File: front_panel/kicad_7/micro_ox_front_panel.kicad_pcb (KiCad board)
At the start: 2 copper layers, 323.8 x 177.8 mm, 8 parts

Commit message: Progress on circuit boards
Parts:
- removed REF** (x8): MountingHole_3.2mm_M3_DIN965, MountingHole:MountingHole_3.2mm_M3_DIN965
- added H1: MountingHole_Pad, MountingHole:MountingHole_3.2mm_M3_Pad_Via, F.Cu at (54.6, 47.0)
- added H2: MountingHole_Pad, MountingHole:MountingHole_3.2mm_M3_Pad_Via, F.Cu at (54.6, 131.4)
- added H3: MountingHole_Pad, MountingHole:MountingHole_3.2mm_M3_Pad_Via, F.Cu at (54.6, 215.9)
- added H4: MountingHole_Pad, MountingHole:MountingHole_3.2mm_M3_Pad_Via, F.Cu at (221.0, 47.0)
- added H5: MountingHole_Pad, MountingHole:MountingHole_3.2mm_M3_Pad_Via, F.Cu at (229.9, 215.9)
- added H6: MountingHole_Pad, MountingHole:MountingHole_3.2mm_M3_Pad_Via, F.Cu at (369.6, 47.0)
- added H7: MountingHole_Pad, MountingHole:MountingHole_3.2mm_M3_Pad_Via, F.Cu at (369.6, 131.4)
- added H8: MountingHole_Pad, MountingHole:MountingHole_3.2mm_M3_Pad_Via, F.Cu at (369.6, 215.9)
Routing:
- added copper zone on B.Cu, net GND
- added copper zone on F.Cu, net GND
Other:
- outline, holes or cut-outs redrawn

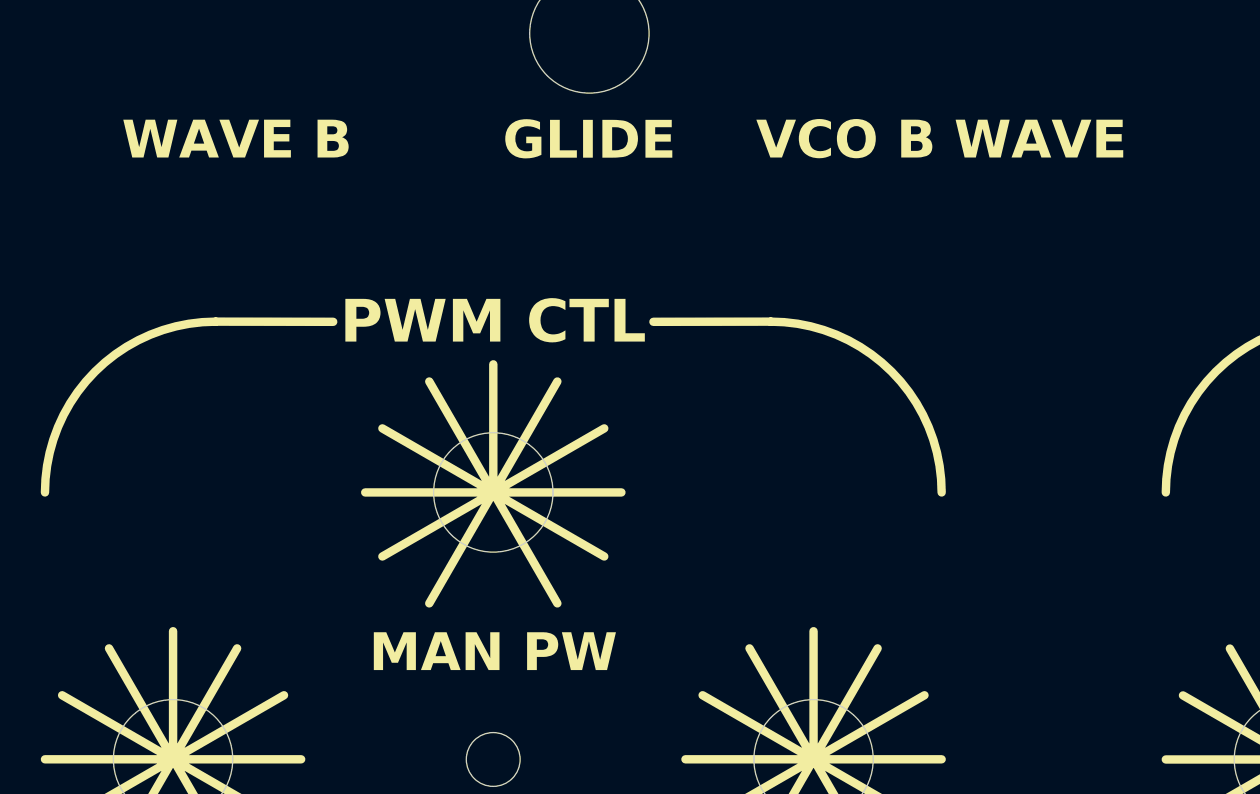
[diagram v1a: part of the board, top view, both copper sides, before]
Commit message: Tweaks to front panel, fix some copy-paste errors
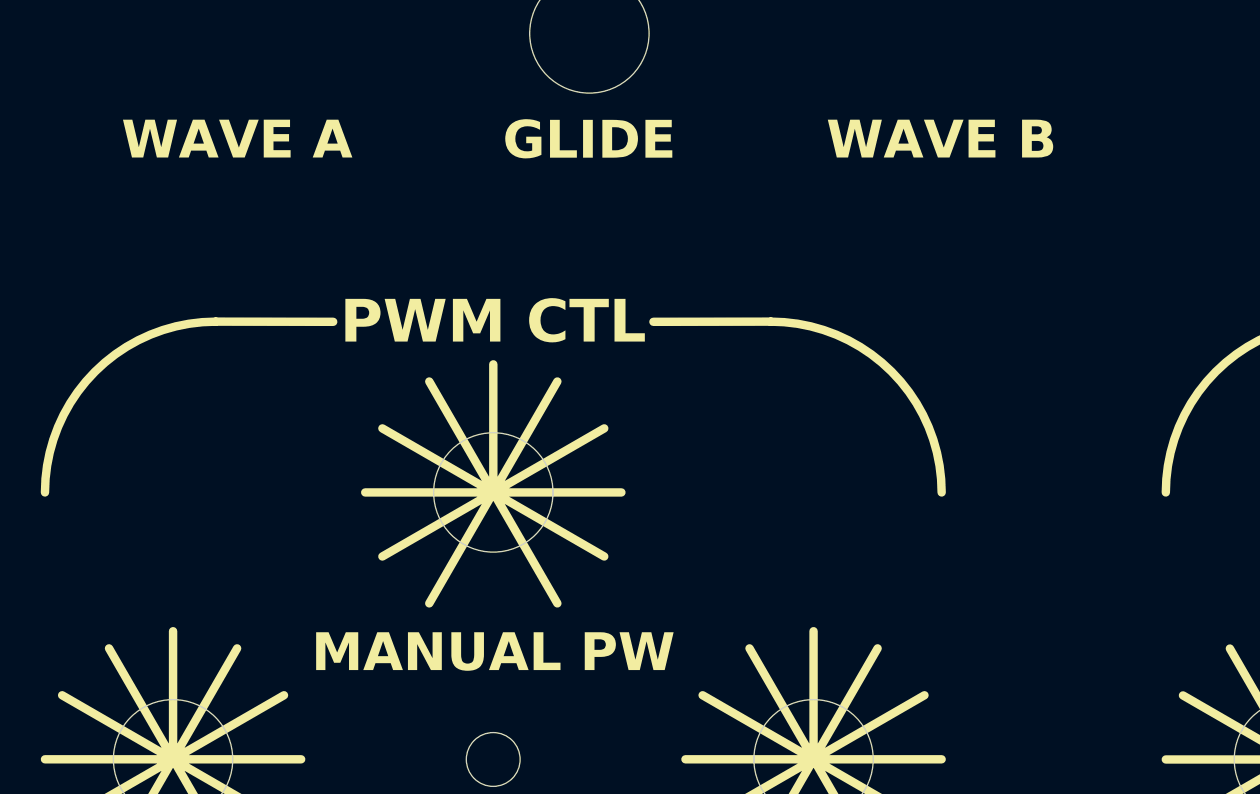
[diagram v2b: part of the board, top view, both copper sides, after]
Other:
- board text added: "MANUAL PW"
- board text added: "WAVE A"
- board text removed: "MAN PW"
- board text removed: "VCO B WAVE"

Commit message: Update front panel
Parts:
- moved H6 3.18 mm to (372.7, 47.0)
- moved H7 3.18 mm to (372.7, 131.4)
- moved H8 3.18 mm to (372.7, 215.9)
- moved H1 3.17 mm to (51.4, 47.0)
- moved H2 3.17 mm to (51.4, 131.4)
- moved H3 3.17 mm to (51.4, 215.9)
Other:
- board size 323.8 x 177.8 mm -> 330.2 x 177.8 mm
- board text added: "JLCJLCJLCJLC"
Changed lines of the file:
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@@
   (title_block
     (title "Micro-Ox front panel")
-    (date "2023-04-13")
+    (date "2023-04-23")
     (rev "0")
     (comment 1 "creativecommons.org/licenses/by/4.0/")
@@
   (net 1 "GND")
   (footprint "MountingHole:MountingHole_3.2mm_M3_Pad_Via" (layer "F.Cu")
-    (at 54.61 131.445)
+    (at 51.435 131.445)
     (descr "Mounting Hole 3.2mm, M3")
     (tags "mounting hole 3.2mm m3")
@@
   )
   (footprint "MountingHole:MountingHole_3.2mm_M3_Pad_Via" (layer "F.Cu")
-    (at 54.61 46.99)
+    (at 51.435 46.99)
     (descr "Mounting Hole 3.2mm, M3")
     (tags "mounting hole 3.2mm m3")
@@
   )
   (footprint "MountingHole:MountingHole_3.2mm_M3_Pad_Via" (layer "F.Cu")
-    (at 369.57 215.9)
+    (at 372.745 215.9)
     (descr "Mounting Hole 3.2mm, M3")
     (tags "mounting hole 3.2mm m3")
@@
   )
   (footprint "MountingHole:MountingHole_3.2mm_M3_Pad_Via" (layer "F.Cu")
-    (at 369.57 46.99)
+    (at 372.745 46.99)
     (descr "Mounting Hole 3.2mm, M3")
     (tags "mounting hole 3.2mm m3")
@@
   )
   (footprint "MountingHole:MountingHole_3.2mm_M3_Pad_Via" (layer "F.Cu")
-    (at 54.61 215.9)
+    (at 51.435 215.9)
     (descr "Mounting Hole 3.2mm, M3")
     (tags "mounting hole 3.2mm m3")
@@
   )
   (footprint "MountingHole:MountingHole_3.2mm_M3_Pad_Via" (layer "F.Cu")
-    (at 369.57 131.445)
+    (at 372.745 131.445)
     (descr "Mounting Hole 3.2mm, M3")
     (tags "mounting hole 3.2mm m3")
@@
   (gr_circle (center 203.2 188.585119) (end 206.75 188.585119)
     (stroke (width 0.05) (type solid)) (fill none) (layer "Edge.Cuts"))
-  (gr_rect (start 50.165 42.545) (end 374.015 220.345)
+  (gr_rect (start 46.99 42.545) (end 377.19 220.345)
     (stroke (width 0.1) (type default)) (fill none) (layer "Edge.Cuts"))
   (gr_rect (start 154.46 113.475) (end 157.96 121.475)
@@
   (gr_circle (center 322.58 161.895357) (end 326.13 161.895357)
     (stroke (width 0.05) (type solid)) (fill none) (layer "Edge.Cuts"))
+  (gr_text "JLCJLCJLCJLC" (at 66.04 45.085) (layer "B.SilkS")
+    (effects (font (size 1 1) (thickness 0.15)) (justify left bottom mirror))
+  )
   (gr_text "RELEASE" (at 337.185 128.230476) (layer "F.SilkS" knockout)
     (effects (font (face "Liberation Sans") (size 2.25 2.25) (thickness 0.2) bold))
